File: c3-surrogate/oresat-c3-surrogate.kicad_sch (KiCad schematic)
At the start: 72 parts, among them J1 J-SAMTEC-TFM-120-X1-XXX-D-RA, J2 Conn_01x04, J4 Conn_01x02_Socket, Q1 PMV45EN, Q3 NTR4101P, Q4 NTR2101P, Q5 DMP3050LVT-7, SW2 Slide Switch, SW3 OS203011MV9QS1, SW4 EG1218, U1 MAX892LEUA+T, U2 LTC4412xS6, U4 LTC4412xS6, U5 TS5A21366, U6 Trinket-M0

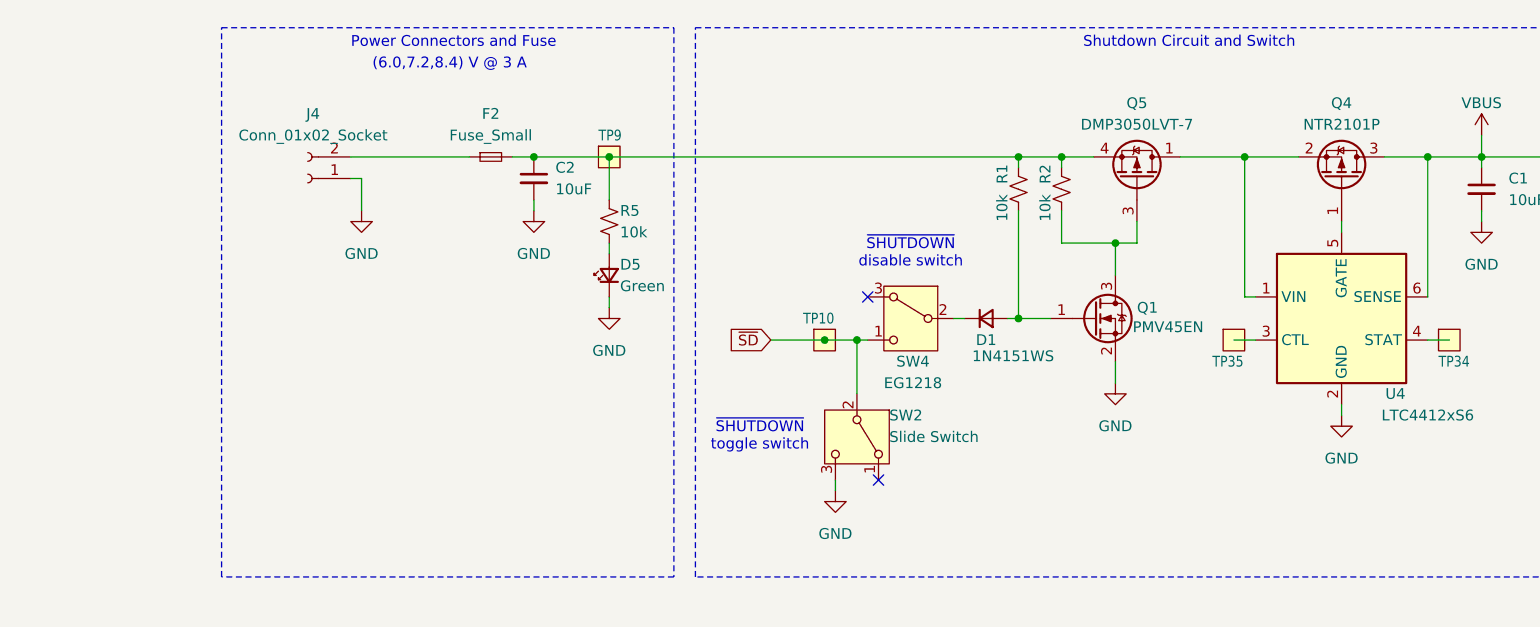
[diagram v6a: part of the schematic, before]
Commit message: made design review corrections to schematic and pcb
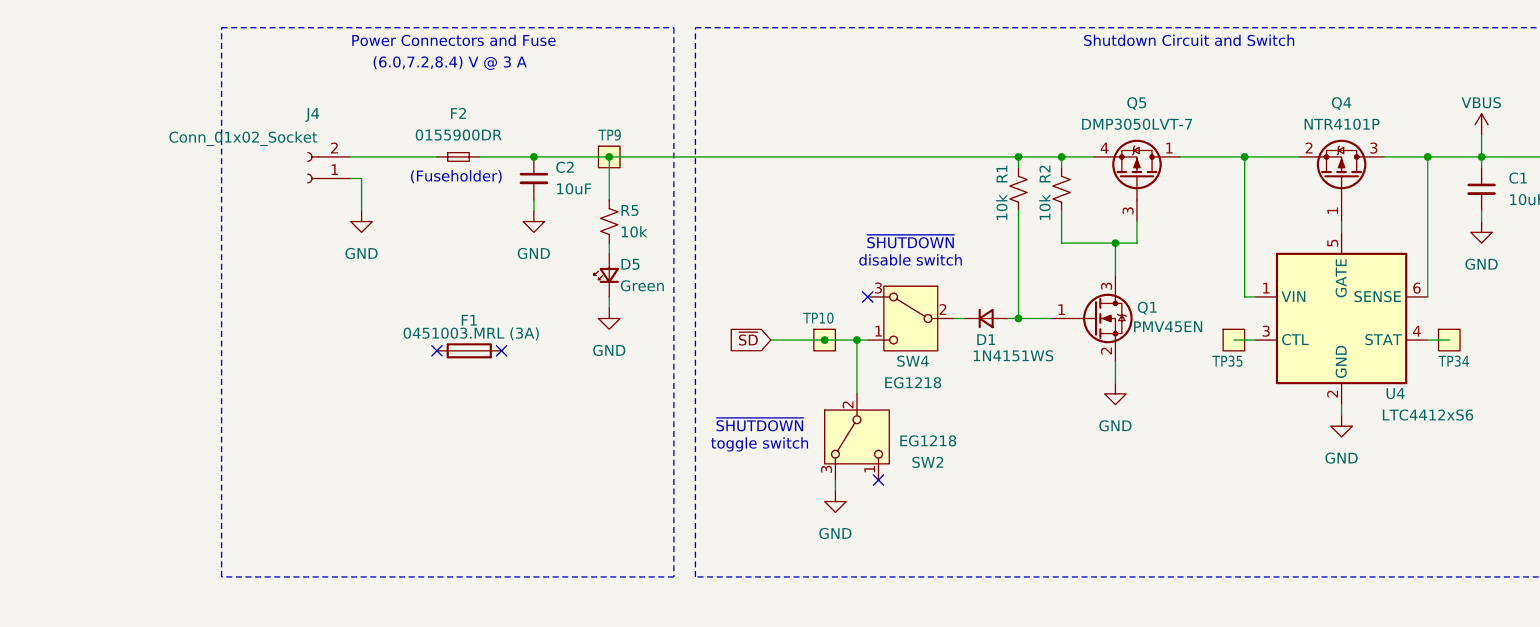
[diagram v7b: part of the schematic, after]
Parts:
- removed SW2: Slide Switch, S-CK-AYZ0102AGRLC-Slide-Switch:AYZ0102AGRLC, symbol Switch:SW_SPDT
- added F1: 0451003.MRL (3A), symbol Device:Fuse
- added SW2: EG1218, Connector_PinHeader_2.54mm:PinHeader_1x03_P2.54mm_Vertical, symbol Switch:SW_SPDT_321
- F2: value Fuse_Small -> 0155900DR
- Q4: value NTR2101P -> NTR4101P
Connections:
- net GND: now also SW2.3 (A)
- net ~{SD}: now also SW2.2 (B)
- no-connect marks 12 -> 14
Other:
- note added: "(Fuseholder)"
- moved on the sheet: F2
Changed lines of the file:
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@@
 	)
 	(no_connect
+		(at 93.98 58.42)
+	)
+	(no_connect
 		(at 144.78 52.07)
 	)
@@
 	)
 	(no_connect
+		(at 101.6 58.42)
+	)
+	(no_connect
 		(at 134.62 152.4)
 	)
@@
 	(wire
 		(pts
-			(xy 83.82 35.56) (xy 97.79 35.56)
+			(xy 83.82 35.56) (xy 93.98 35.56)
 		)
 		(stroke
@@
 	(wire
 		(pts
-			(xy 102.87 35.56) (xy 105.41 35.56)
+			(xy 99.06 35.56) (xy 105.41 35.56)
 		)
 		(stroke
@@
 		)
 	)
+	(text "(Fuseholder)\n"
+		(exclude_from_sim no)
+		(at 96.266 38.1 0)
+		(effects
+			(font
+				(size 1.27 1.27)
+			)
+		)
+	)
 	(text "VulCAN USB to CAN Adapter\n\n"
 		(exclude_from_sim no)
@@
 			)
 		)
-		(property "Value" "NTR2101P"
+		(property "Value" "NTR4101P"
 			(at 200.66 31.75 90)
 			(effects
@@
 	(symbol
 		(lib_id "Device:Fuse_Small")
-		(at 100.33 35.56 0)
+		(at 96.52 35.56 0)
 		(unit 1)
 		(exclude_from_sim no)
@@
 		(fields_autoplaced yes)
 		(property "Reference" "F2"
-			(at 100.33 30.48 0)
+			(at 96.52 30.48 0)
 			(effects
 				(font
@@
 			)
 		)
-		(property "Value" "Fuse_Small"
-			(at 100.33 33.02 0)
+		(property "Value" "0155900DR"
+			(at 96.52 33.02 0)
 			(effects
 				(font
@@
 		)
 		(property "Footprint" "oresat-passives:Littelfuse 155900DR"
-			(at 100.33 35.56 0)
+			(at 96.52 35.56 0)
 			(effects
 				(font
@@
 		)
 		(property "Datasheet" "~"
-			(at 100.33 35.56 0)
+			(at 96.52 35.56 0)
 			(effects
 				(font
@@
 		)
 		(property "Description" "Fuse, small symbol"
-			(at 100.33 35.56 0)
+			(at 96.52 35.56 0)
 			(effects
 				(font
@@
 	)
 	(symbol
-		(lib_id "Switch:SW_SPDT")
-		(at 143.51 68.58 270)
-		(unit 1)
-		(exclude_from_sim no)
-		(in_bom yes)
-		(on_board yes)
-		(dnp no)
-		(property "Reference" "SW2"
-			(at 147.32 66.04 90)
-			(effects
-				(font
-					(size 1.27 1.27)
-				)
-				(justify left)
-			)
-		)
-		(property "Value" "Slide Switch"
-			(at 147.32 68.58 90)
-			(effects
-				(font
-					(size 1.27 1.27)
-				)
-				(justify left)
-			)
-		)
-		(property "Footprint" "S-CK-AYZ0102AGRLC-Slide-Switch:AYZ0102AGRLC"
-			(at 143.51 68.58 0)
-			(effects
-				(font
-					(size 1.27 1.27)
-				)
-				(hide yes)
-			)
-		)
-		(property "Datasheet" "~"
-			(at 143.51 68.58 0)
-			(effects
-				(font
-					(size 1.27 1.27)
-				)
-				(hide yes)
-			)
-		)
-		(property "Description" "Switch, single pole double throw"
-			(at 143.51 68.58 0)
-			(effects
-				(font
-					(size 1.27 1.27)
-				)
-				(hide yes)
-			)
-		)
-		(property "DIST" "Digi-Key"
-			(at 143.51 68.58 0)
-			(effects
-				(font
-					(size 1.27 1.27)
-				)
-				(hide yes)
-			)
-		)
-		(property "DPN" "401-2012-1-ND"
-			(at 143.51 68.58 0)
-			(effects
-				(font
-					(size 1.27 1.27)
-				)
-				(hide yes)
-			)
-		)
-		(property "MFR" "C&K"
-			(at 143.51 68.58 0)
-			(effects
-				(font
-					(size 1.27 1.27)
-				)
-				(hide yes)
-			)
-		)
-		(property "MPN" "AYZ0102AGRLC"
-			(at 143.51 68.58 0)
-			(effects
-				(font
-					(size 1.27 1.27)
-				)
-				(hide yes)
-			)
-		)
-		(pin "1"
-		)
-		(pin "2"
-		)
-		(pin "3"
-		)
-		(instances
-			(project "oresat-c3-surrogate"
-				(path "/a762bfd7-2da3-46cd-8ea9-3793bee7a19f"
-					(reference "SW2")
-					(unit 1)
-				)
-			)
-		)
-	)
-	(symbol
 		(lib_name "GND_2")
 		(lib_id "power:GND")
@@
 		(on_board yes)
 		(dnp no)
-		(fields_autoplaced yes)
 		(property "Reference" "J4"
 			(at 79.375 30.48 0)
@@
 		)
 		(property "Value" "Conn_01x02_Socket"
-			(at 79.375 33.02 0)
+			(at 71.12 33.274 0)
 			(effects
 				(font
@@
 	)
 	(symbol
+		(lib_id "Device:Fuse")
+		(at 97.79 58.42 90)
+		(unit 1)
+		(exclude_from_sim no)
+		(in_bom yes)
+		(on_board no)
+		(dnp no)
+		(property "Reference" "F1"
+			(at 97.79 54.864 90)
+			(effects
+				(font
+					(size 1.27 1.27)
+				)
+			)
+		)
+		(property "Value" "0451003.MRL (3A)"
+			(at 98.044 56.388 90)
+			(effects
+				(font
+					(size 1.27 1.27)
+				)
+			)
+		)
+		(property "Footprint" ""
+			(at 97.79 60.198 90)
+			(effects
+				(font
+					(size 1.27 1.27)
+				)
+				(hide yes)
+			)
+		)
+		(property "Datasheet" "https://www.littelfuse.com/media?resourcetype=datasheets&itemid=533cd5cc-956c-4243-867f-6ab5a62f6ba1&filename=littelfuse_fuse_451_453_datasheet.pdf"
+			(at 97.79 58.42 0)
+			(effects
+				(font
+					(size 1.27 1.27)
+				)
+				(hide yes)
+			)
+		)
+		(property "Description" "Fuse"
+			(at 97.79 58.42 0)
+			(effects
+				(font
+					(size 1.27 1.27)
+				)
+				(hide yes)
+			)
+		)
+		(property "DPN" "F2583CT-ND"
+			(at 97.79 58.42 0)
+			(effects
+				(font
+					(size 1.27 1.27)
+				)
+				(hide yes)
+			)
+		)
+		(property "MPN" "0451003.MRL"
+			(at 97.79 58.42 0)
+			(effects
+				(font
+					(size 1.27 1.27)
+				)
+				(hide yes)
+			)
+		)
+		(property "DST" "Digi-Key"
+			(at 97.79 58.42 0)
+			(effects
+				(font
+					(size 1.27 1.27)
+				)
+				(hide yes)
+			)
+		)
+		(property "MFR" "LittelFuse"
+			(at 97.79 58.42 0)
+			(effects
+				(font
+					(size 1.27 1.27)
+				)
+				(hide yes)
+			)
+		)
+		(pin "2"
+		)
+		(pin "1"
+		)
+		(instances
+			(project "oresat-c3-surrogate"
+				(path "/a762bfd7-2da3-46cd-8ea9-3793bee7a19f"
+					(reference "F1")
+					(unit 1)
+				)
+			)
+		)
+	)
+	(symbol
 		(lib_id "oresat-ics:TS5A21366")
 		(at 241.3 182.88 0)
@@
 					(unit 1)
 				)
+			)
+		)
+	)
+	(symbol
+		(lib_id "Switch:SW_SPDT_321")
+		(at 143.51 68.58 90)
+		(mirror x)
+		(unit 1)
+		(exclude_from_sim no)
+		(in_bom yes)
+		(on_board yes)
+		(dnp no)
+		(property "Reference" "SW2"
+			(at 151.892 71.628 90)
+			(effects
+				(font
+					(size 1.27 1.27)
+				)
+			)
+		)
+		(property "Value" "EG1218"
+			(at 151.892 69.088 90)
+			(effects
+				(font
+					(size 1.27 1.27)
+				)
+			)
+		)
+		(property "Footprint" "Connector_PinHeader_2.54mm:PinHeader_1x03_P2.54mm_Vertical"
+			(at 153.67 68.58 0)
+			(effects
+				(font
+					(size 1.27 1.27)
+				)
+				(hide yes)
+			)
+		)
+		(property "Datasheet" "https://sten-eswitch-13110800-production.s3.amazonaws.com/system/asset/product_line/data_sheet/119/EG.pdf"
+			(at 151.13 68.58 0)
+			(effects
+				(font
+					(size 1.27 1.27)
+				)
+				(hide yes)
+			)
+		)
+		(property "Description" "Switch, single pole double throw"
+			(at 143.51 68.58 0)
+			(effects
+				(font
+					(size 1.27 1.27)
+				)
+				(hide yes)
+			)
+		)
+		(property "DPN" "EG1903-ND"
+			(at 143.51 68.58 0)
+			(effects
+				(font
+					(size 1.27 1.27)
+				)
+				(hide yes)
+			)
+		)
+		(property "DST" "Digi-Key"
+			(at 143.51 68.58 0)
+			(effects
+				(font
+					(size 1.27 1.27)
+				)
+				(hide yes)
+			)
+		)
+		(property "MFR" "E-Switch"
+			(at 143.51 68.58 0)
+			(effects
+				(font
+					(size 1.27 1.27)
+				)
+				(hide yes)
+			)
+		)
+		(property "MPN" "EG1218"
+			(at 143.51 68.58 0)
+			(effects
+				(font
+					(size 1.27 1.27)
+				)
+				(hide yes)
+			)
+		)
+		(pin "3"
+		)
+		(pin "2"
+		)
+		(pin "1"
+		)
+		(instances
+			(project "oresat-c3-surrogate"
+				(path "/a762bfd7-2da3-46cd-8ea9-3793bee7a19f"
+					(reference "SW2")
+					(unit 1)
+				)

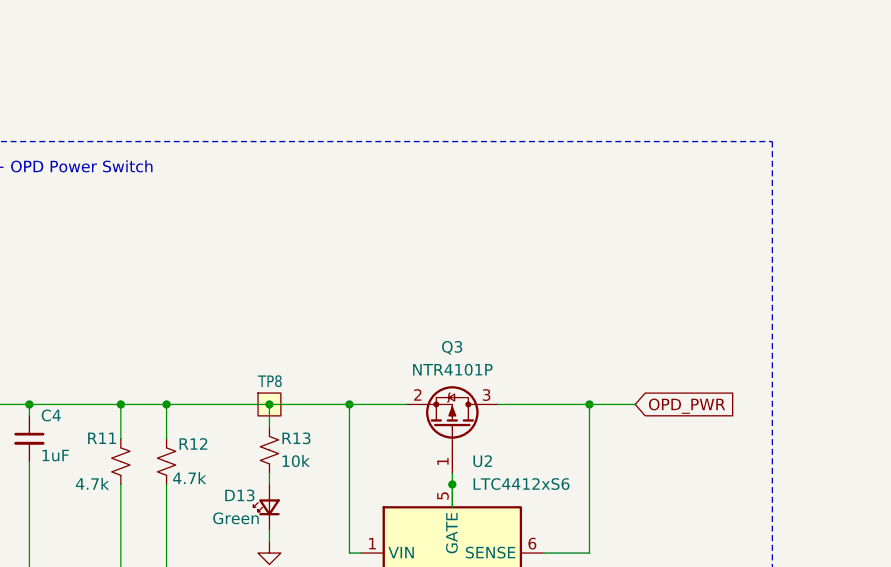
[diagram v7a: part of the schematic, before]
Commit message: edited via size, rearranged tracks
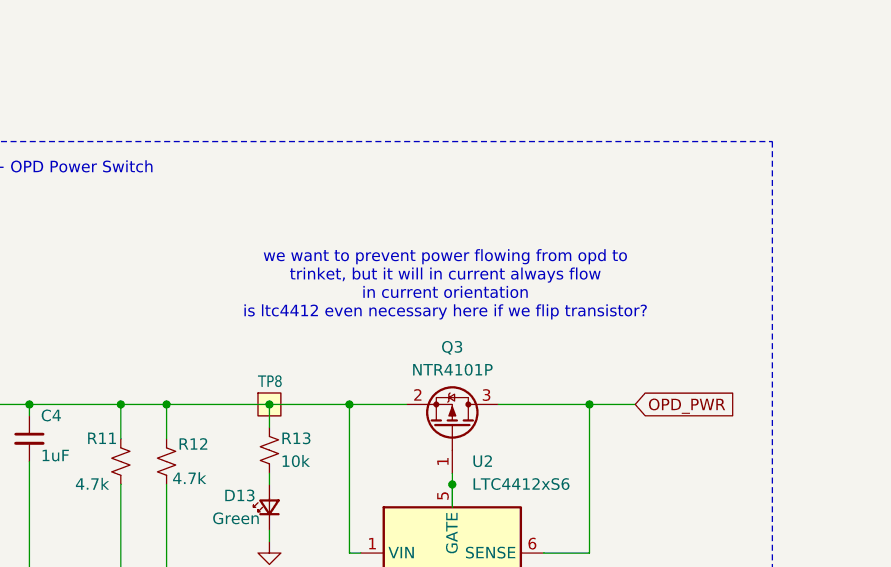
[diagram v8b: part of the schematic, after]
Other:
- note added: "we want to prevent power flowing from opd to trinket, but it will in current always flow in current orientation is ltc4412 even necessary here if we flip transistor?"
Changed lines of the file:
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@@
+		)
+	)
+	(text "we want to prevent power flowing from opd to \ntrinket, but it will in current always flow \nin current orientation\nis ltc4412 even necessary here if we flip transistor?"
+		(exclude_from_sim no)
+		(at 240.538 118.872 0)
+		(effects
+			(font
+				(size 1.27 1.27)
+			)
 		)
 	)
